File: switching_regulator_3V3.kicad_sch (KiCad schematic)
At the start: 19 parts, among them U24 tps54331DR

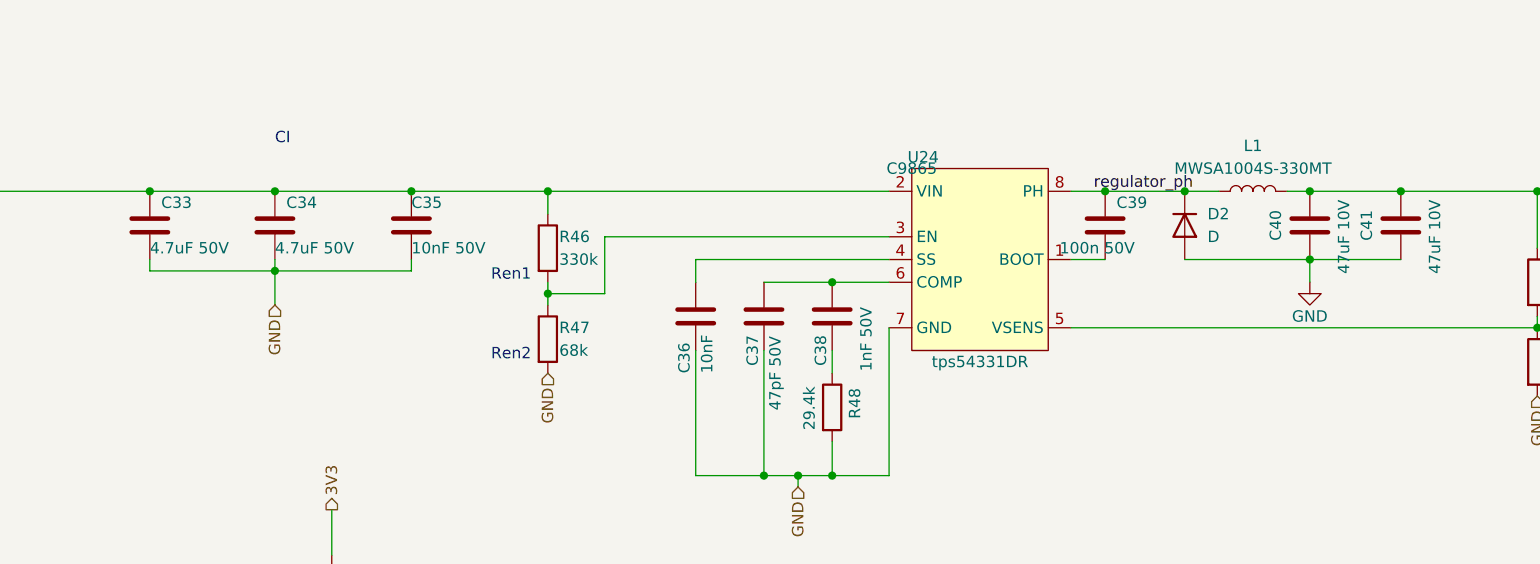
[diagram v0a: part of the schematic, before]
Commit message: Keyed stepper drivers. Larger input connector
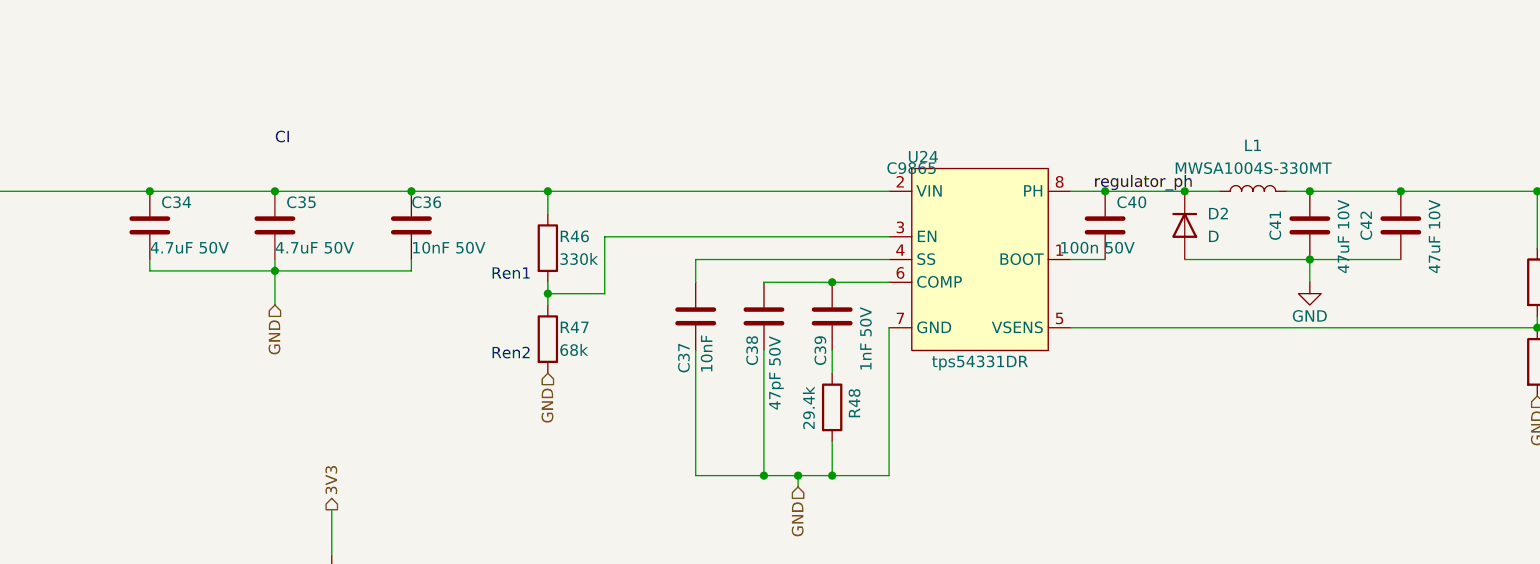
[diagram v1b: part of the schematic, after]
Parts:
- renumbered C33 to C34, C34 to C35, C35 to C36, C36 to C37, C37 to C38, C38 to C39, C39 to C40, C40 to C41, C41 to C42
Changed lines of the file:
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@@
   (symbol (lib_id "Device:C") (at 83.82 107.95 0) (unit 1)
     (in_bom yes) (on_board yes)
-    (property "Reference" "C35" (id 0) (at 83.82 105.41 0)
+    (property "Reference" "C36" (id 0) (at 83.82 105.41 0)
       (effects (font (size 1.27 1.27)) (justify left))
     )
@@
   (symbol (lib_id "Device:C") (at 54.61 107.95 0) (unit 1)
     (in_bom yes) (on_board yes)
-    (property "Reference" "C33" (id 0) (at 55.88 105.41 0)
+    (property "Reference" "C34" (id 0) (at 55.88 105.41 0)
       (effects (font (size 1.27 1.27)) (justify left))
     )
@@
   (symbol (lib_id "Device:C") (at 130.81 118.11 0) (unit 1)
     (in_bom yes) (on_board yes)
-    (property "Reference" "C38" (id 0) (at 129.54 121.92 90))
+    (property "Reference" "C39" (id 0) (at 129.54 121.92 90))
     (property "Value" "1nF 50V" (id 1) (at 134.62 120.65 90))
     (property "Footprint" "Capacitor_SMD:C_0402_1005Metric" (id 2) (at 131.7752 121.92 0)
@@
   (symbol (lib_id "Device:C") (at 194.31 107.95 180) (unit 1)
     (in_bom yes) (on_board yes)
-    (property "Reference" "C41" (id 0) (at 190.5 107.95 90))
+    (property "Reference" "C42" (id 0) (at 190.5 107.95 90))
     (property "Value" "47uF 10V" (id 1) (at 198.12 109.22 90))
     (property "Footprint" "Capacitor_SMD:C_1206_3216Metric" (id 2) (at 193.3448 104.14 0)
@@
   (symbol (lib_id "Device:C") (at 68.58 107.95 0) (unit 1)
     (in_bom yes) (on_board yes)
-    (property "Reference" "C34" (id 0) (at 69.85 105.41 0)
+    (property "Reference" "C35" (id 0) (at 69.85 105.41 0)
       (effects (font (size 1.27 1.27)) (justify left))
     )
@@
   (symbol (lib_id "Device:C") (at 184.15 107.95 180) (unit 1)
     (in_bom yes) (on_board yes)
-    (property "Reference" "C40" (id 0) (at 180.34 107.95 90))
+    (property "Reference" "C41" (id 0) (at 180.34 107.95 90))
     (property "Value" "47uF 10V" (id 1) (at 187.96 109.22 90))
     (property "Footprint" "Capacitor_SMD:C_1206_3216Metric" (id 2) (at 183.1848 104.14 0)
@@
   (symbol (lib_id "Device:C") (at 161.29 107.95 0) (unit 1)
     (in_bom yes) (on_board yes)
-    (property "Reference" "C39" (id 0) (at 162.56 105.41 0)
+    (property "Reference" "C40" (id 0) (at 162.56 105.41 0)
       (effects (font (size 1.27 1.27)) (justify left))
     )
@@
   (symbol (lib_id "Device:C") (at 123.19 118.11 0) (unit 1)
     (in_bom yes) (on_board yes)
-    (property "Reference" "C37" (id 0) (at 121.92 121.92 90))
+    (property "Reference" "C38" (id 0) (at 121.92 121.92 90))
     (property "Value" "47pF 50V" (id 1) (at 124.46 124.46 90))
     (property "Footprint" "Capacitor_SMD:C_0402_1005Metric" (id 2) (at 124.1552 121.92 0)
@@
   (symbol (lib_id "Device:C") (at 115.57 118.11 0) (unit 1)
     (in_bom yes) (on_board yes)
-    (property "Reference" "C36" (id 0) (at 114.3 124.46 90)
-      (effects (font (size 1.27 1.27)) (justify left))
-    )
+    (property "Reference" "C37" (id 0) (at 114.3 124.46 90)
+      (effects (font (size 1.27 1.27)) (justify left))
+    )
